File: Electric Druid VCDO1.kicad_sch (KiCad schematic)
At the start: 18 parts, among them J1 EURO_PWR_16P, J2 EuroPower_JST_3P, U1 L7805, U2 L7905, U3 VCDO1

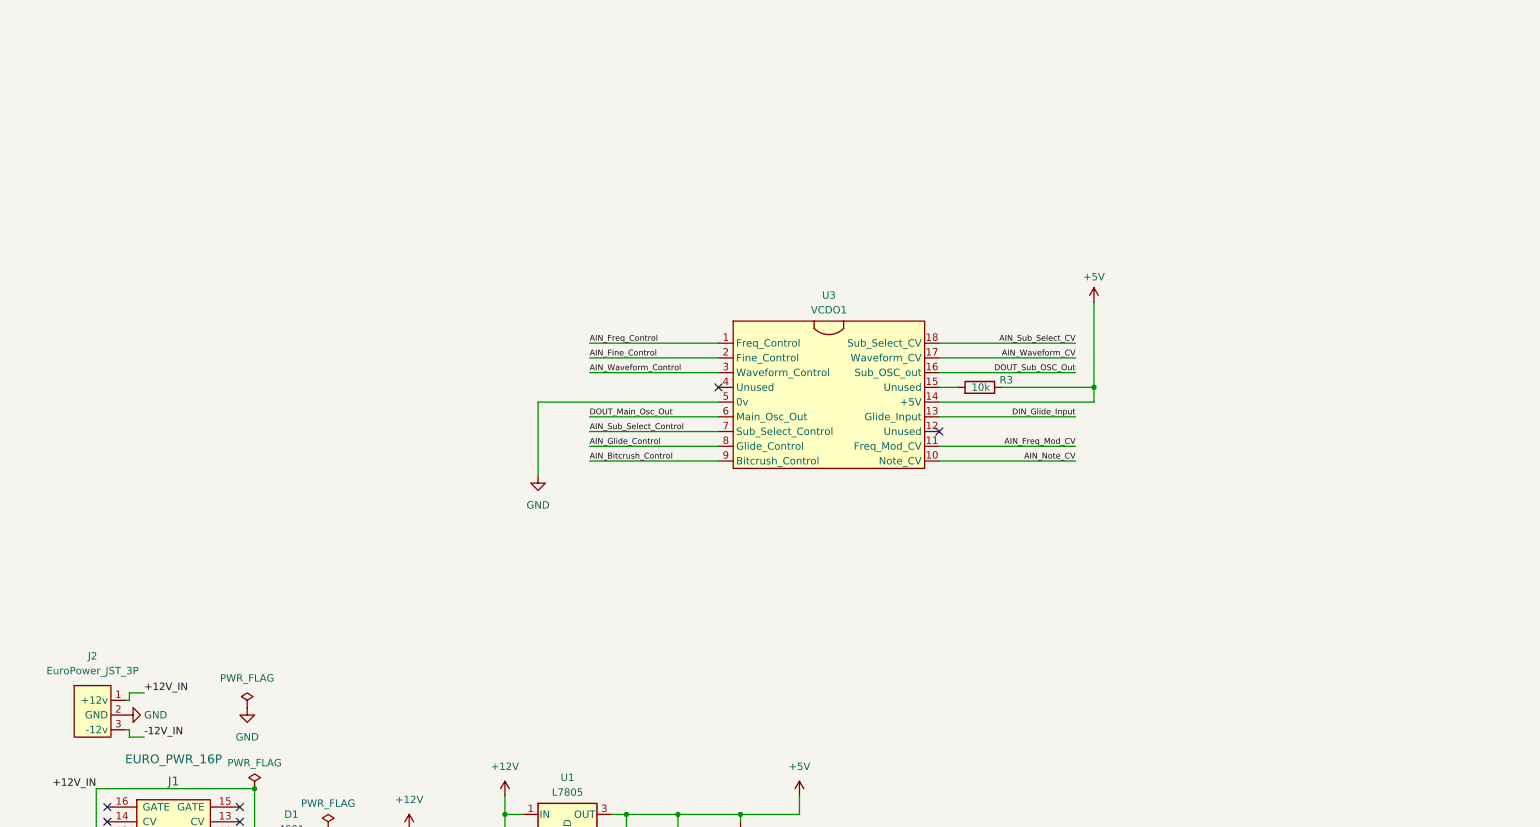
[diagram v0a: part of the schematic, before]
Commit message: Schematic rev0.1 update
glide in, output filters done
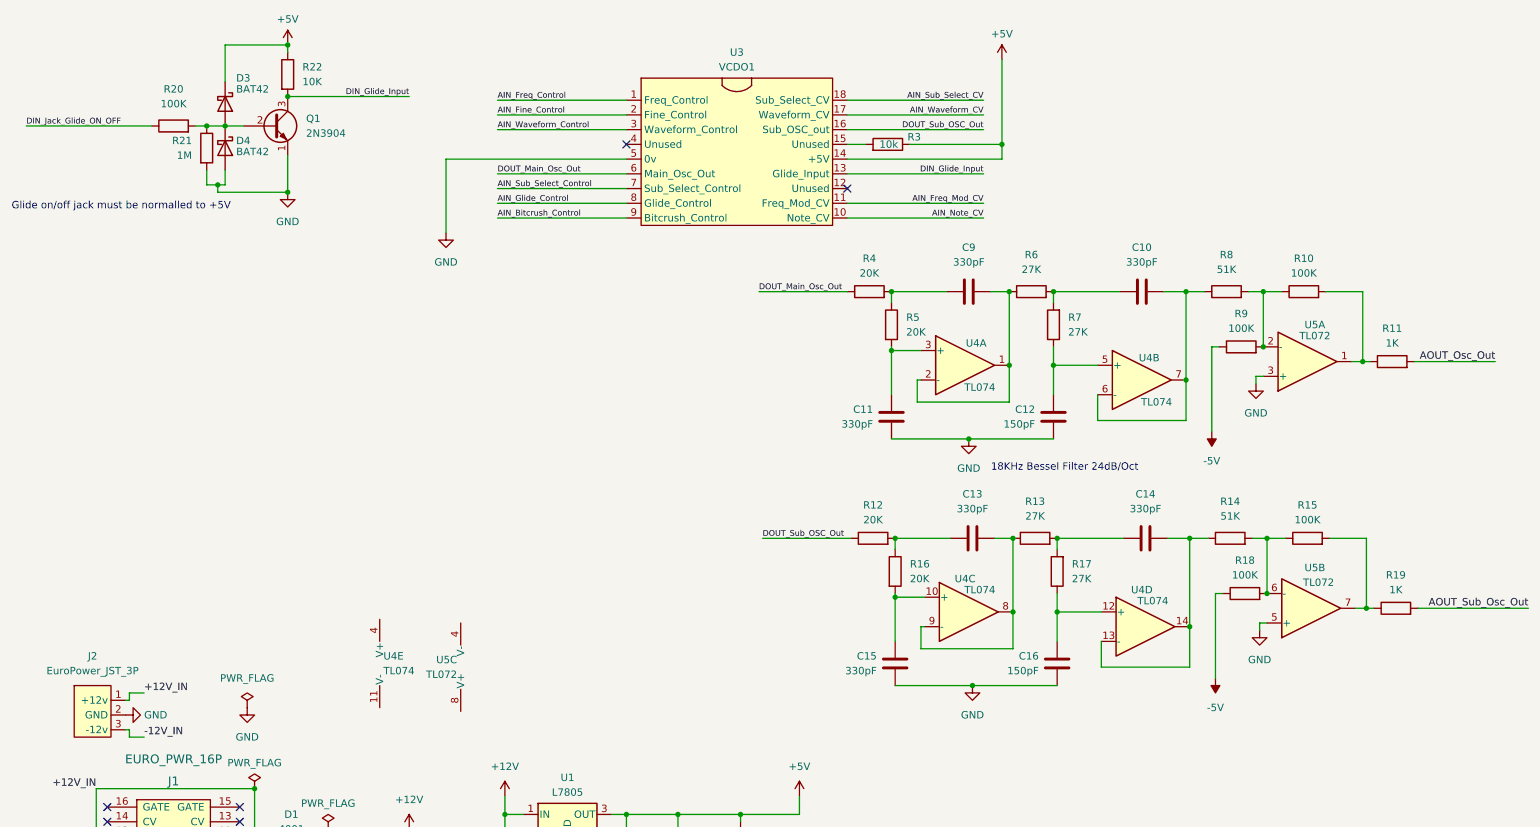
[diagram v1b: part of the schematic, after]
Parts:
- added C10, C11, C13, C14, C15, C9: 330pF, symbol Device:C
- added C12, C16: 150pF, symbol Device:C
- added D3, D4: BAT42, Diode_THT:D_DO-35_SOD27_P7.62mm_Horizontal, symbol Diode:BAT42
- added Q1: 2N3904, Package_TO_SOT_THT:TO-92_Inline, symbol Transistor_BJT:2N3904
- added R10, R15, R18, R20, R9: 100K, symbol Device:R
- added R11, R19: 1K, symbol Device:R
- added R12, R16, R4, R5: 20K, symbol Device:R
- added R13, R17, R6, R7: 27K, symbol Device:R
- added R14, R8: 51K, symbol Device:R
- added R21: 1M, symbol Device:R
- added R22: 10K, symbol Device:R
- added U4: TL074, symbol Amplifier_Operational:TL074
- added U5: TL072, symbol Amplifier_Operational:TL072
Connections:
- net +5V: now also D3.1 (K), R22.1
- net -5V: now also R18.1, R9.1
- net DIN_Glide_Input: now also Q1.3 (C), R22.2
- net DOUT_Main_Osc_Out: now also R4.1
- net DOUT_Sub_OSC_Out: now also R12.1
- net GND: now also C11.1, C12.1, C15.1, C16.1, D4.2 (A), Q1.1 (E), R21.2, U5.3 (+), U5.5 (+)
- new net: C9.1, R4.2, R5.1
- new net: C9.2, R6.1, U4.1, U4.2 (-)
- new net: D3.2 (A), D4.1 (K), Q1.2 (B), R20.2, R21.1
- new net: C15.2, R16.2, U4.10 (+)
- new net: C13.1, R12.2, R16.1
- new net: C16.2, R17.1, U4.12 (+)
- new net: R14.2, R15.1, R18.2, U5.6 (-)
- new net: R10.1, R8.2, R9.2, U5.2 (-)
- new net: R10.2, R11.1, U5.1
- new net: C11.2, R5.2, U4.3 (+)
- new net: C10.1, R6.2, R7.2
- new net: C10.2, R8.1, U4.6 (-), U4.7
- new net: C14.2, R14.1, U4.13 (-), U4.14
- new net: C14.1, R13.2, R17.2
- new net: C12.2, R7.1, U4.5 (+)
- new net: C13.2, R13.1, U4.8, U4.9 (-)
- new net: R15.2, R19.1, U5.7
- new net AOUT_Osc_Out: R11.2
- new net AOUT_Sub_Osc_Out: R19.2
- new net DIN_Jack_Glide_ON_OFF: R20.1
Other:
- note added: "18KHz Bessel Filter 24dB/Oct"
- note added: "Glide on/off jack must be normalled to +5V"
- moved on the sheet: R3, U3

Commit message: Root page filled with circuit
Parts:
- added C17, C18, C19, C20, C21, C22, C23, C24, C25: 0.1uF, symbol Device:C
- added D10, D11, D12, D5, D6, D7, D8, D9: BAT42, Diode_THT:D_DO-35_SOD27_P7.62mm_Horizontal, symbol Diode:BAT42
- added J3: Main_osc_out, symbol DIYSynthMNL:PJ3001F
- added J4: Sub_osc_out, symbol DIYSynthMNL:PJ3001F
- added J5: Glide_on_off_in, symbol DIYSynthMNL:PJ3001F
- added J6: Note_CV_in, symbol DIYSynthMNL:PJ3001F
- added J7: Freq_Mod_CV_in, symbol DIYSynthMNL:PJ3001F
- added J8: Wave_CV_in, symbol DIYSynthMNL:PJ3001F
- added J9: Spare_CV, symbol DIYSynthMNL:PJ3001F
- added R23: 10K, symbol Device:R
- added R24, R27: 91K, symbol Device:R
- added R25, R29, R33, R37: 100K, symbol Device:R
- added R26, R31, R34, R38: 4K7, symbol Device:R
- added R28, R32, R35, R36, R39: 200K, symbol Device:R
- added R30: 180K, symbol Device:R
- added R40, R41, R42, R43, R44, R45: 1K, symbol Device:R
- added RV1: 20K_1V/Oct_Adjust, symbol Device:R_Potentiometer_Trim
- added RV10: 10K_SubWaveSel, symbol Device:R_Potentiometer
- added RV11: 10K_Glide, symbol Device:R_Potentiometer
- added RV12: 10K_Bitcrush, symbol Device:R_Potentiometer
- added RV2: 20K_Offset_trim, symbol Device:R_Potentiometer_Trim
- added RV3: 100K_FM_CV_Amount, symbol Device:R_Potentiometer
- added RV4: 47K_Zero_Trim, symbol Device:R_Potentiometer_Trim
- added RV5: 100K_WaveSel_CV_Amount, symbol Device:R_Potentiometer
- added RV6: 100K_SubSel_CV_Amount, symbol Device:R_Potentiometer
- added RV7: 10K_Freq_Course, symbol Device:R_Potentiometer
- added RV8: 10K_Freq_Fine, symbol Device:R_Potentiometer
- added RV9: 10K_MainWaveSel, symbol Device:R_Potentiometer
- added U6: TL074, symbol Amplifier_Operational:TL074
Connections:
- net +12V: now also U4.4 (V+), U5.8 (V+), C17.1, C18.1, C19.1, U6.4 (V+)
- net +5V: now also D11.1 (K), D5.1 (K), D7.1 (K), D9.1 (K), R23.1, RV10.3, RV11.3, RV12.3, RV7.3, RV8.3, RV9.3
- net -12V: now also U4.11 (V-), U5.4 (V-), C17.2, C18.2, C19.2, U6.11 (V-)
- net -5V: now also R35.1, R39.1, RV2.1, RV4.1
- net AIN_Freq_Mod_CV: now also D7.2 (A), D8.1 (K), R31.2
- net AIN_Note_CV: now also D5.2 (A), D6.1 (K), R26.2
- net AIN_Sub_Select_CV: now also D11.2 (A), D12.1 (K), R38.2
- net AIN_Waveform_CV: now also D10.1 (K), D9.2 (A), R34.2
- net GND: now also C20.2, C21.2, C22.2, C23.2, C24.2, C25.2, D10.2 (A), D12.2 (A), D6.2 (A), D8.2 (A), J3.S, J4.S, J5.S, J6.S, J7.S, J8.S, J9.S, RV10.1, RV11.1, RV12.1, RV3.1, RV5.1, RV6.1, RV7.1, RV8.1, RV9.1, U6.10 (+), U6.12 (+), U6.3 (+), U6.5 (+)
- net AIN_Sub_Select_Control renamed AIN_Sub_Wave_Select_Control
- net AIN_Waveform_Control renamed AIN_Waveform_Select_Control
- net AOUT_Osc_Out renamed AOUT_Jack_Osc_Out
- net AOUT_Sub_Osc_Out renamed AOUT_Jack_Sub_Osc_Out
- new net: R40.2, RV7.2
- new net: R24.2, RV1.1
- new net: R25.1, R27.2, RV1.2, RV1.3, U6.2 (-)
- new net: R25.2, R26.1, U6.1
- new net: R28.2, R29.1, R30.2, U6.6 (-)
- new net: R29.2, R31.1, U6.7
- new net: R41.2, RV8.2
- new net: R28.1, RV3.2
- new net: R36.2, R37.1, R39.2, U6.13 (-)
- new net: R37.2, R38.1, U6.14
- new net: R43.2, RV10.2
- new net: R44.2, RV11.2
- new net: R36.1, RV6.2
- new net: R30.1, RV4.2, RV4.3
- new net: R33.2, R34.1, U6.8
- new net: R32.1, RV5.2
- new net: R32.2, R33.1, R35.2, U6.9 (-)
- new net: J5.TN, R23.2
- new net: R42.2, RV9.2
- new net: R45.2, RV12.2
- new net: R27.1, RV2.2, RV2.3
- new net AIN_Jack_Freq_Mod_CV: RV3.3
- new net AIN_Jack_Freq_Mod_CV_B2: J7.T
- new net AIN_Jack_MainWave_Select_CV_B2: J8.T
- new net AIN_Jack_Note_CV: R24.1
- new net AIN_Jack_Note_CV_B2: J6.T
- new net AIN_Jack_SubWave_Select_CV_B2: J9.T
- new net AIN_Jack_Sub_Select_CV: RV6.3
- new net AIN_Jack_Wave_Select_CV: RV5.3
- new net AIN_Pot_Bitcrush_Control: C25.1, R45.1
- new net AIN_Pot_Freq_Course_Control: C20.1, R40.1
- new net AIN_Pot_Freq_Fine_Control: C21.1, R41.1
- new net AIN_Pot_Glide_Control: C24.1, R44.1
- new net AIN_Pot_MainWaveSel_Control: C22.1, R42.1
- new net AIN_Pot_SubWaveSel_Control: C23.1, R43.1
- new net AOUT_Jack_Osc_Out_B2: J3.T
- new net AOUT_Jack_Sub_Osc_Out_B2: J4.T
- new net DIN_Jack_Glide_ON_OFF_B2: J5.T
- no-connect marks 8 -> 14
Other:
- note added: "+/-5V"
- note added: "0V-5V"
- note added: "0V/5V"
- note added: "CV=Jacks Control=Pots"
- note added: "Controls/Pots"
- note added: "Glide on/off jack must be normalled to +5V through a 10K ohm pullup resistor"
- note added: "Inputs"
- note added: "Outputs"
- note added: "Power"
- note added: "Try MCP6004 in place of U6 and change the circuit"
- note removed: "Glide on/off jack must be normalled to +5V"
- moved on the sheet: C1, C10, C11, C12, C13, C14, C15, C16, C2, C3, C4, C5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

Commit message: added bitcrush and glide cv inputs
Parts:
- removed C24, C25: 0.1uF, symbol Device:C
- removed R44, R45: 1K, symbol Device:R
- removed RV11: 10K_Glide, symbol Device:R_Potentiometer
- removed RV12: 10K_Bitcrush, symbol Device:R_Potentiometer
- added D13, D14, D15, D16: BAT42, Diode_THT:D_DO-35_SOD27_P7.62mm_Horizontal, symbol Diode:BAT42
- added J10: Glide_time_cv, symbol DIYSynthMNL:PJ3001F
- added J11: Bitcrush_cv, symbol DIYSynthMNL:PJ3001F
- added R46, R49, R50, R53: 200K, symbol Device:R
- added R47, R51: 100K, symbol Device:R
- added R48, R52: 4K7, symbol Device:R
- added RV13: 100K_GlideTime_CV_Amount, symbol Device:R_Potentiometer
- added RV14: 100K_Glide, symbol Device:R_Potentiometer
- added RV15: 100K_Bitcrush, symbol Device:R_Potentiometer
- added RV16: 100K_Bitcrush_CV_Amount, symbol Device:R_Potentiometer
- added U7: TL072, symbol Amplifier_Operational:TL072
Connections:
- net +5V: now also D13.1 (K), D15.1 (K), RV14.3, RV15.3
- net -5V: now also R49.1, R53.1, RV14.1, RV15.1
- net AIN_Pot_Bitcrush_Control: now also D15.2 (A), D16.1 (K), R52.2
- net AIN_Pot_Glide_Control: now also D13.2 (A), D14.1 (K), R48.2
- net GND: now also D14.2 (A), D16.2 (A), J10.S, J11.S, RV13.1, RV16.1, U7.3 (+), U7.5 (+)
- new net: J10.TN, RV14.2
- new net: R50.1, RV16.2
- new net: R50.2, R51.1, R53.2, U7.6 (-)
- new net: R46.1, RV13.2
- new net: R47.2, R48.1, U7.1
- new net: J11.TN, RV15.2
- new net: R46.2, R47.1, R49.2, U7.2 (-)
- new net: R51.2, R52.1, U7.7
- new net AIN_Jack_Bitcrush_CV: RV16.3
- new net AIN_Jack_Bitcrush_CV_B2: J11.T
- new net AIN_Jack_GlideTime_CV: RV13.3
- new net AIN_Jack_GlideTime_CV_B2: J10.T
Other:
- note added: "10vpp in"
- note removed: "Try MCP6004 in place of U6 and change the circuit"
- moved on the sheet: C1, C17, C18, C19, C2, C20, C21, C22, C23, C3, C4, C5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

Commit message: Circuit rev0.1 finished
I'll move on next to doing the different sheets for the multiboard workflow.
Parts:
- added C24: 0.1uF, symbol Device:C
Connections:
- net +12V: now also U7.8 (V+), C24.1
- net -12V: now also U7.4 (V-), C24.2
- net AIN_Jack_Bitcrush_CV: now also R50.1; no longer RV16.3
- net AIN_Jack_Bitcrush_CV_B2: now also RV16.2; no longer J11.T
- net AIN_Jack_Freq_Mod_CV: now also R28.1; no longer RV3.3
- net AIN_Jack_Freq_Mod_CV_B2: now also RV3.2; no longer J7.T
- net AIN_Jack_GlideTime_CV: now also R46.1; no longer RV13.3
- net AIN_Jack_GlideTime_CV_B2: now also RV13.2; no longer J10.T
- net AIN_Jack_MainWave_Select_CV_B2: now also RV5.2; no longer J8.T
- net AIN_Jack_SubWave_Select_CV_B2: now also RV6.2; no longer J9.T
- net AIN_Jack_Sub_Select_CV: now also R36.1; no longer RV6.3
- net AIN_Jack_Wave_Select_CV: now also R32.1; no longer RV5.3
- new net: J9.T, RV6.3
- new net: J10.T, RV13.3
- new net: J7.T, RV3.3
- new net: J8.T, RV5.3
- new net: J11.T, RV16.3
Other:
- note added: "Bitcrush CV"
- note added: "FM CV"
- note added: "Glide CV"
- note added: "Glide on/off CV"
- note added: "Input processing/conversion to 0v to 5v"
- note added: "Main Wave Select CV"
- note added: "Main oscillator"
- note added: "Note CV"
- note added: "Output processing"
- note added: "Outputs jacks"
- note added: "Pots inverted on purpose!"
- note added: "Sub Wave Select CV"
- note added: "Sub oscillator"
- note removed: "Outputs"
- moved on the sheet: C1, C10, C11, C12, C13, C14, C15, C16, C17, C18, C19, C2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

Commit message: Multiboard work update
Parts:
- removed C1, C2: 22uF, symbol Device:C_Polarized
- removed C10, C11, C13, C14, C15, C9: 330pF, symbol Device:C
- removed C12, C16: 150pF, symbol Device:C
- removed C17, C18, C19, C20, C21, C22, C23, C24: 0.1uF, symbol Device:C
- removed C3, C4, C6, C7: 2.2uF, symbol Device:C_Polarized
- removed C5, C8: 100nF, symbol Device:C
- removed D1, D2: 4001, symbol Device:D
- removed D10, D11, D12, D13, D14, D15, D16, D3, D4, D5, D6, D7, D8, D9: BAT42, Diode_THT:D_DO-35_SOD27_P7.62mm_Horizontal, symbol Diode:BAT42
- removed J1: EURO_PWR_16P, symbol DIYSynthMNL:EURO_PWR_16_PIN
- removed J10: Glide_time_cv, symbol DIYSynthMNL:PJ3001F
- removed J11: Bitcrush_cv, symbol DIYSynthMNL:PJ3001F
- removed J2: EuroPower_JST_3P, symbol DIYSynthMNL:JST_Eurorack_power_3P
- removed J3: Main_osc_out, symbol DIYSynthMNL:PJ3001F
- removed J4: Sub_osc_out, symbol DIYSynthMNL:PJ3001F
- removed J5: Glide_on_off_in, symbol DIYSynthMNL:PJ3001F
- removed J6: Note_CV_in, symbol DIYSynthMNL:PJ3001F
- removed J7: Freq_Mod_CV_in, symbol DIYSynthMNL:PJ3001F
- removed J8: Wave_CV_in, symbol DIYSynthMNL:PJ3001F
- removed J9: Spare_CV, symbol DIYSynthMNL:PJ3001F
- removed Q1: 2N3904, Package_TO_SOT_THT:TO-92_Inline, symbol Transistor_BJT:2N3904
- removed R1, R2: *10k, symbol Device:R
- removed R10, R15, R18, R20, R25, R29, R33, R37, R47, R51, R9: 100K, symbol Device:R
- removed R11, R19, R40, R41, R42, R43: 1K, symbol Device:R
- removed R12, R16, R4, R5: 20K, symbol Device:R
- removed R13, R17, R6, R7: 27K, symbol Device:R
- removed R14, R8: 51K, symbol Device:R
- removed R21: 1M, symbol Device:R
- removed R22, R23: 10K, symbol Device:R
- removed R24, R27: 91K, symbol Device:R
- removed R26, R31, R34, R38, R48, R52: 4K7, symbol Device:R
- removed R28, R32, R35, R36, R39, R46, R49, R50, R53: 200K, symbol Device:R
- removed R3: 10k, symbol Device:R
- removed R30: 180K, symbol Device:R
- removed RV1: 20K_1V/Oct_Adjust, symbol Device:R_Potentiometer_Trim
- removed RV10: 10K_SubWaveSel, symbol Device:R_Potentiometer
- removed RV13: 100K_GlideTime_CV_Amount, symbol Device:R_Potentiometer
- removed RV14: 100K_Glide, symbol Device:R_Potentiometer
- removed RV15: 100K_Bitcrush, symbol Device:R_Potentiometer
- removed RV16: 100K_Bitcrush_CV_Amount, symbol Device:R_Potentiometer
- removed RV2: 20K_Offset_trim, symbol Device:R_Potentiometer_Trim
- removed RV3: 100K_FM_CV_Amount, symbol Device:R_Potentiometer
- removed RV4: 47K_Zero_Trim, symbol Device:R_Potentiometer_Trim
- removed RV5: 100K_WaveSel_CV_Amount, symbol Device:R_Potentiometer
- removed RV6: 100K_SubSel_CV_Amount, symbol Device:R_Potentiometer
- removed RV7: 10K_Freq_Course, symbol Device:R_Potentiometer
- removed RV8: 10K_Freq_Fine, symbol Device:R_Potentiometer
- removed RV9: 10K_MainWaveSel, symbol Device:R_Potentiometer
- removed U1: L7805, symbol Regulator_Linear:L7805
- removed U2: L7905, symbol Regulator_Linear:L7905
- removed U3: VCDO1, symbol DIYSynthMNL:Druid_VCDO1_PIC16F1847
- removed U4, U6: TL074, symbol Amplifier_Operational:TL074
- removed U5, U7: TL072, symbol Amplifier_Operational:TL072
- added J12: Control_board, Connector_PinHeader_2.54mm:PinHeader_1x16_P2.54mm_Vertical, symbol Connector:Conn_01x16_Pin
- added J13: Main_board, Connector_PinSocket_2.54mm:PinSocket_1x16_P2.54mm_Vertical, symbol Connector:Conn_01x16_Socket
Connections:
- new net Eurorack_Electric_Druid_VCDO1_Control_Board/Bitcrush_CV: J12.11 (Pin_11)
- new net Eurorack_Electric_Druid_VCDO1_Control_Board/CB_+5V: J12.14 (Pin_14)
- new net Eurorack_Electric_Druid_VCDO1_Control_Board/CB_-5V: J12.16 (Pin_16)
- new net Eurorack_Electric_Druid_VCDO1_Control_Board/CB_GND: J12.15 (Pin_15)
- new net Eurorack_Electric_Druid_VCDO1_Control_Board/FM_CV: J12.6 (Pin_6)
- new net Eurorack_Electric_Druid_VCDO1_Control_Board/Freq_Course_Ctrl: J12.1 (Pin_1)
- new net Eurorack_Electric_Druid_VCDO1_Control_Board/Freq_Fine_Ctrl: J12.2 (Pin_2)
- new net Eurorack_Electric_Druid_VCDO1_Control_Board/Glide_OnOff_CV: J12.9 (Pin_9)
- new net Eurorack_Electric_Druid_VCDO1_Control_Board/Glide_Time_CV: J12.10 (Pin_10)
- new net Eurorack_Electric_Druid_VCDO1_Control_Board/MainOsc_Out: J12.12 (Pin_12)
- new net Eurorack_Electric_Druid_VCDO1_Control_Board/MainWaveSel_CV: J12.8 (Pin_8)
- new net Eurorack_Electric_Druid_VCDO1_Control_Board/MainWaveSel_Ctrl: J12.3 (Pin_3)
- new net Eurorack_Electric_Druid_VCDO1_Control_Board/Note_CV: J12.5 (Pin_5)
- new net Eurorack_Electric_Druid_VCDO1_Control_Board/SubOsc_Out: J12.13 (Pin_13)
- new net Eurorack_Electric_Druid_VCDO1_Control_Board/SubWaveSel_CV: J12.7 (Pin_7)
- new net Eurorack_Electric_Druid_VCDO1_Control_Board/SubWaveSel_Ctrl: J12.4 (Pin_4)
- new net Eurorack_Electric_Druid_VCDO1_Main_Board/+5V: J13.14 (Pin_14)
- new net Eurorack_Electric_Druid_VCDO1_Main_Board/-5V: J13.16 (Pin_16)
- new net Eurorack_Electric_Druid_VCDO1_Main_Board/Bitcrush_CV: J13.11 (Pin_11)
- new net Eurorack_Electric_Druid_VCDO1_Main_Board/FM_CV: J13.6 (Pin_6)
- new net Eurorack_Electric_Druid_VCDO1_Main_Board/Freq_Course_Ctrl: J13.1 (Pin_1)
- new net Eurorack_Electric_Druid_VCDO1_Main_Board/Freq_Fine_Ctrl: J13.2 (Pin_2)
- new net Eurorack_Electric_Druid_VCDO1_Main_Board/GND: J13.15 (Pin_15)
- new net Eurorack_Electric_Druid_VCDO1_Main_Board/GlideTime_CV: J13.10 (Pin_10)
- new net Eurorack_Electric_Druid_VCDO1_Main_Board/Glide_OnOff_CV: J13.9 (Pin_9)
- new net Eurorack_Electric_Druid_VCDO1_Main_Board/MainOsc_Out: J13.12 (Pin_12)
- new net Eurorack_Electric_Druid_VCDO1_Main_Board/MainWaveSel_CV: J13.8 (Pin_8)
- new net Eurorack_Electric_Druid_VCDO1_Main_Board/MainWaveSel_Ctrl: J13.3 (Pin_3)
- new net Eurorack_Electric_Druid_VCDO1_Main_Board/Note_CV: J13.5 (Pin_5)
- new net Eurorack_Electric_Druid_VCDO1_Main_Board/SubOsc_Out: J13.13 (Pin_13)
- new net Eurorack_Electric_Druid_VCDO1_Main_Board/SubWaveSel_CV: J13.7 (Pin_7)
- new net Eurorack_Electric_Druid_VCDO1_Main_Board/SubWaveSel_Ctrl: J13.4 (Pin_4)
- no-connect marks 14 -> 0
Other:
- sheet Eurorack_Electric_Druid_VCDO1_Control_Board ports: added Bitcrush_CV, CB_+5V, CB_-5V, CB_GND, FM_CV, Freq_Course_Ctrl, Freq_Fine_Ctrl, Glide_OnOff_CV, Glide_Time_CV, MainOsc_Out, MainWaveSel_CV, MainWaveSel_Ctrl, Note_CV, SubOsc_Out, SubWaveSel_CV, SubWaveSel_Ctrl; removed none
- sheet Eurorack_Electric_Druid_VCDO1_Main_Board ports: added +5V, -5V, Bitcrush_CV, FM_CV, Freq_Course_Ctrl, Freq_Fine_Ctrl, GND, GlideTime_CV, Glide_OnOff_CV, MainOsc_Out, MainWaveSel_CV, MainWaveSel_Ctrl, Note_CV, SubOsc_Out, SubWaveSel_CV, SubWaveSel_Ctrl; removed none
- note removed: "*Optional Load Resistor"
- note removed: "+/-5V"
- note removed: "0V-5V"
- note removed: "0V/5V"
- note removed: "10vpp in"
- note removed: "18KHz Bessel Filter 24dB/Oct"
- note removed: "Bitcrush CV"
- note removed: "CV=Jacks Control=Pots"
- note removed: "Controls/Pots"
- note removed: "FM CV"
- note removed: "Glide CV"
- note removed: "Glide on/off CV"
- note removed: "Glide on/off jack must be normalled to +5V through a 10K ohm pullup resistor"
- note removed: "Input processing/conversion to 0v to 5v"
- note removed: "Inputs"
- note removed: "Main Wave Select CV"
- note removed: "Main oscillator"
- note removed: "Note CV"
- note removed: "Output processing"
- note removed: "Outputs jacks"
- note removed: "Pots inverted on purpose!"
- note removed: "Power"
- note removed: "Sub Wave Select CV"
- note removed: "Sub oscillator"
- note removed: "The Druid datasheet has a design error with the negative 5 volt regulator."
